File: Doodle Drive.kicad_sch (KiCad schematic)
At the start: 49 parts, among them J1 USB_B, J2 PINHD_1x4_Male, J6 PINHD_1x2_Male, SW1 Push_Button, SW2 Push_Button, SW3 Push_Button, U1 STM32F411RETx, U6 AP7343-30W5-7, U7 CP2102N-Axx-xQFN28, Y1 32.768KHz ±20ppm 12.5pF, Y2 25MHZ 9PF

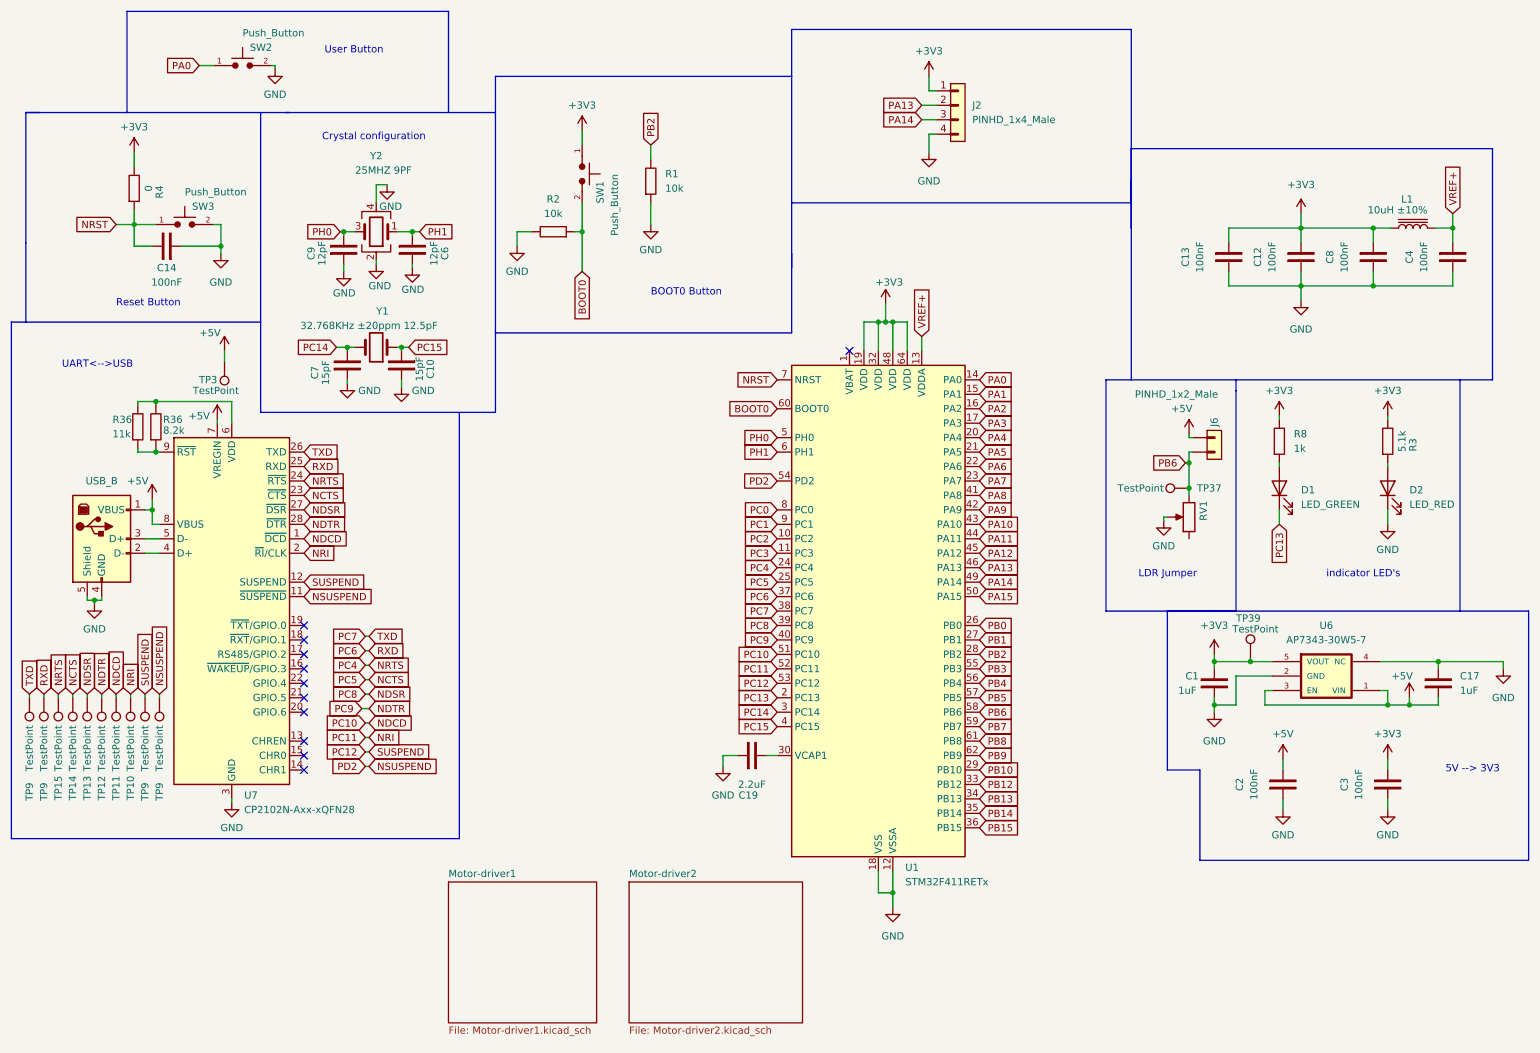
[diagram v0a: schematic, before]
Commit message: temporarly detached testpoints
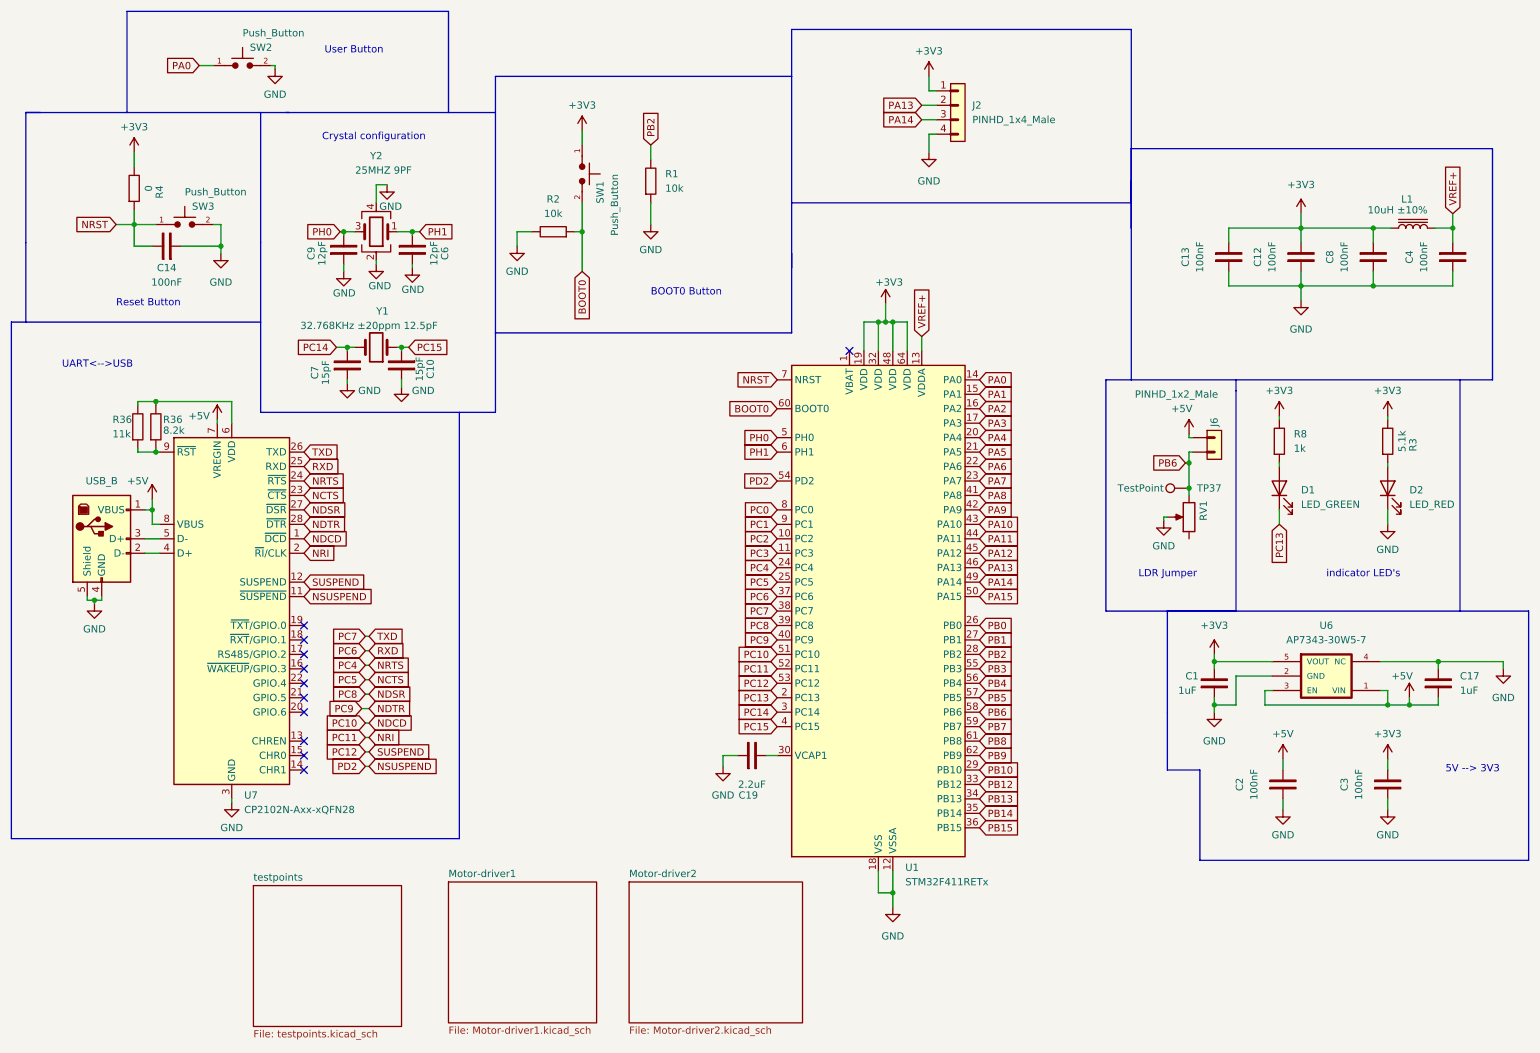
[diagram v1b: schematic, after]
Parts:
- removed TP10, TP11, TP12, TP13, TP14, TP15, TP3, TP39, TP9 (x4): TestPoint, TestPoint:TestPoint_Pad_D2.5mm, symbol Connector:TestPoint
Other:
- added sheet testpoints (testpoints.kicad_sch)

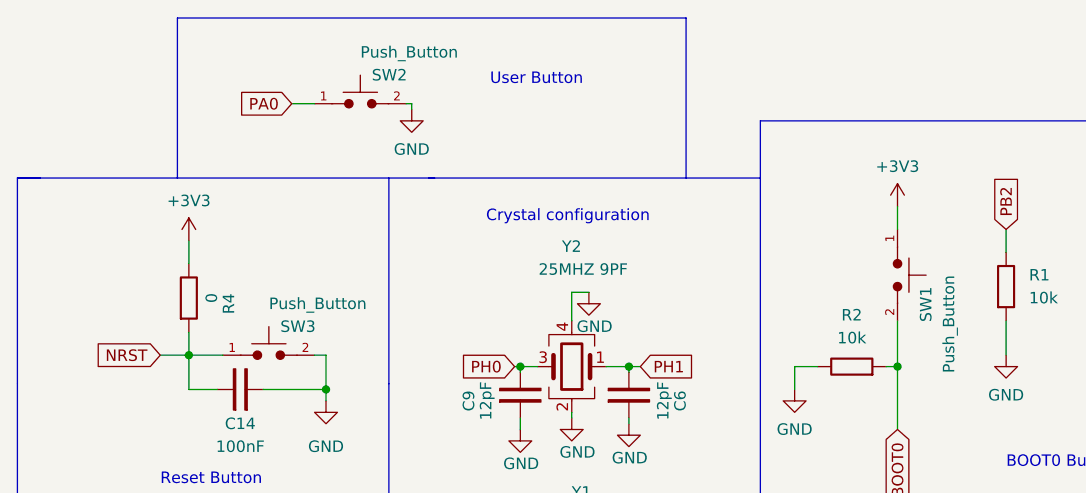
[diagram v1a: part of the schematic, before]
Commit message: routet Motor Driver modules, reattached and placed testpoints
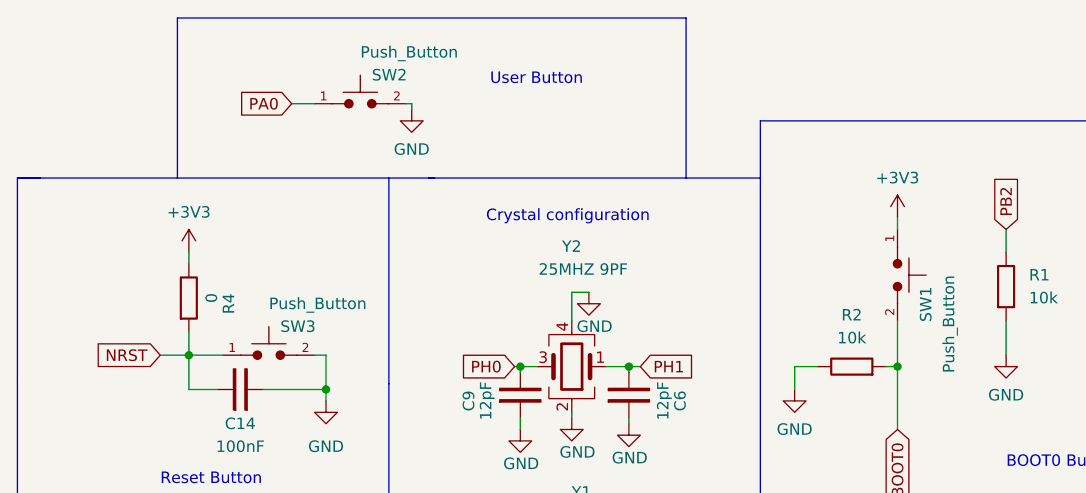
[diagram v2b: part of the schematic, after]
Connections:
- net +3.3V is gone; now on net +3V3: R4.2, SW1.1
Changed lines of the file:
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@@
-    (stroke (width 0) (type default))
-  )
-  (wire (pts (xy 37.465 40.005) (xy 37.465 37.465))
     (stroke (width 0) (type default))
   )
@@
     (stroke (width 0) (type default))
   )
+  (wire (pts (xy 116.205 34.925) (xy 116.205 36.195))
+    (stroke (width 0) (type default))
+  )
   (wire (pts (xy 266.7 127) (xy 266.7 128.27))
     (stroke (width 0) (type default))
@@
     (stroke (width 0) (type default))
   )
-  (wire (pts (xy 116.205 36.195) (xy 116.205 33.655))
-    (stroke (width 0) (type default))
-  )
   (wire (pts (xy 104.775 51.435) (xy 104.775 53.975))
     (stroke (width 0) (type default))
@@
   )
   (wire (pts (xy 86.36 51.435) (xy 83.82 51.435))
+    (stroke (width 0) (type default))
+  )
+  (wire (pts (xy 37.465 38.735) (xy 37.465 40.005))
     (stroke (width 0) (type default))
   )
@@
     )
   )
+  (symbol (lib_id "power:+3V3") (at 37.465 38.735 0) (unit 1)
+    (in_bom yes) (on_board yes) (dnp no) (fields_autoplaced)
+    (property "Reference" "#PWR024" (at 37.465 42.545 0)
+      (effects (font (size 1.27 1.27)) hide)
+    )
+    (property "Value" "+3V3" (at 37.465 34.29 0)
+      (effects (font (size 1.27 1.27)))
+    )
+    (property "Footprint" "" (at 37.465 38.735 0)
+      (effects (font (size 1.27 1.27)) hide)
+    )
+    (property "Datasheet" "" (at 37.465 38.735 0)
+      (effects (font (size 1.27 1.27)) hide)
+    )
+    (pin "1")
+    (instances
+      (project "Doodle Drive"
+        (path "/3ec634aa-8c09-482d-9325-2288a4dbd68b"
+          (reference "#PWR024") (unit 1)
+        )
+      )
+    )
+  )
   (symbol (lib_id "Device:Crystal") (at 80.01 71.755 180) (unit 1)
     (in_bom yes) (on_board yes) (dnp no)
@@
         (path "/3ec634aa-8c09-482d-9325-2288a4dbd68b"
           (reference "R2") (unit 1)
+        )
+      )
+    )
+  )
+  (symbol (lib_id "power:+3V3") (at 116.205 34.925 0) (unit 1)
+    (in_bom yes) (on_board yes) (dnp no) (fields_autoplaced)
+    (property "Reference" "#PWR020" (at 116.205 38.735 0)
+      (effects (font (size 1.27 1.27)) hide)
+    )
+    (property "Value" "+3V3" (at 116.205 30.48 0)
+      (effects (font (size 1.27 1.27)))
+    )
+    (property "Footprint" "" (at 116.205 34.925 0)
+      (effects (font (size 1.27 1.27)) hide)
+    )
+    (property "Datasheet" "" (at 116.205 34.925 0)
+      (effects (font (size 1.27 1.27)) hide)
+    )
+    (pin "1")
+    (instances
+      (project "Doodle Drive"
+        (path "/3ec634aa-8c09-482d-9325-2288a4dbd68b"
+          (reference "#PWR020") (unit 1)
         )
       )
@@
     )
   )
+  (symbol (lib_id "PCM_SL_Devices:Push_Button") (at 116.205 41.275 270) (unit 1)
+    (in_bom yes) (on_board yes) (dnp no)
+    (property "Reference" "SW1" (at 119.38 42.545 0)
+      (effects (font (size 1.27 1.27)) (justify left))
+    )
+    (property "Value" "Push_Button" (at 121.92 41.275 0)
+      (effects (font (size 1.27 1.27)) (justify left))
+    )
+    (property "Footprint" "Button_Switch_SMD:SW_SPST_B3U-1000P" (at 113.03 41.148 0)
+      (effects (font (size 1.27 1.27)) hide)
+    )
+    (property "Datasheet" "" (at 116.205 41.275 0)
+      (effects (font (size 1.27 1.27)) hide)
+    )
+    (pin "1")
+    (pin "2")
+    (instances
+      (project "Doodle Drive"
+        (path "/3ec634aa-8c09-482d-9325-2288a4dbd68b"
+          (reference "SW1") (unit 1)
+        )
+      )
+    )
+  )
   (symbol (lib_id "power:+5V") (at 40.64 98.425 0) (unit 1)
     (in_bom yes) (on_board yes) (dnp no)
@@
     )
   )
-  (symbol (lib_id "PCM_SL_Devices:Push_Button") (at 116.205 41.275 270) (unit 1)
-    (in_bom yes) (on_board yes) (dnp no)
-    (property "Reference" "SW1" (at 119.38 42.545 0)
-      (effects (font (size 1.27 1.27)) (justify left))
-    )
-    (property "Value" "Push_Button" (at 121.92 41.275 0)
-      (effects (font (size 1.27 1.27)) (justify left))
-    )
-    (property "Footprint" "Button_Switch_SMD:SW_SPST_B3U-1000P" (at 113.03 41.148 0)
-      (effects (font (size 1.27 1.27)) hide)
-    )
-    (property "Datasheet" "" (at 116.205 41.275 0)
-      (effects (font (size 1.27 1.27)) hide)
-    )
-    (pin "1")
-    (pin "2")
-    (instances
-      (project "Doodle Drive"
-        (path "/3ec634aa-8c09-482d-9325-2288a4dbd68b"
-          (reference "SW1") (unit 1)
-        )
-      )
-    )
-  )
   (symbol (lib_id "PCM_SL_Devices:Resistor") (at 38.1 85.725 90) (unit 1)
     (in_bom yes) (on_board yes) (dnp no)
@@
         (path "/3ec634aa-8c09-482d-9325-2288a4dbd68b"
           (reference "C9") (unit 1)
+        )
+      )
+    )
+  )
+  (symbol (lib_id "PCM_SL_Devices:Resistor") (at 37.465 43.815 90) (unit 1)
+    (in_bom yes) (on_board yes) (dnp no)
+    (property "Reference" "R4" (at 41.91 44.45 0)
+      (effects (font (size 1.27 1.27)))
+    )
+    (property "Value" "0" (at 40.005 43.815 0)
+      (effects (font (size 1.27 1.27)))
+    )
+    (property "Footprint" "Resistor_SMD:R_0805_2012Metric" (at 41.783 42.926 0)
+      (effects (font (size 1.27 1.27)) hide)
+    )
+    (property "Datasheet" "" (at 37.465 43.307 0)
+      (effects (font (size 1.27 1.27)) hide)
+    )
+    (pin "1")
+    (pin "2")
+    (instances
+      (project "Doodle Drive"
+        (path "/3ec634aa-8c09-482d-9325-2288a4dbd68b"
+          (reference "R4") (unit 1)
         )
       )
@@
     )
   )
-  (symbol (lib_id "power:+3.3V") (at 37.465 37.465 0) (unit 1)
-    (in_bom yes) (on_board yes) (dnp no) (fields_autoplaced)
-    (property "Reference" "#PWR024" (at 37.465 41.275 0)
-      (effects (font (size 1.27 1.27)) hide)
-    )
-    (property "Value" "+3V3" (at 37.465 33.02 0)
-      (effects (font (size 1.27 1.27)))
-    )
-    (property "Footprint" "" (at 37.465 37.465 0)
-      (effects (font (size 1.27 1.27)) hide)
-    )
-    (property "Datasheet" "" (at 37.465 37.465 0)
-      (effects (font (size 1.27 1.27)) hide)
-    )
-    (pin "1")
-    (instances
-      (project "Doodle Drive"
-        (path "/3ec634aa-8c09-482d-9325-2288a4dbd68b"
-          (reference "#PWR024") (unit 1)
-        )
-      )
-    )
-  )
   (symbol (lib_id "power:+3V3") (at 238.76 83.82 0) (unit 1)
     (in_bom yes) (on_board yes) (dnp no)
@@
         (path "/3ec634aa-8c09-482d-9325-2288a4dbd68b"
           (reference "#PWR011") (unit 1)
-        )
-      )
-    )
-  )
-  (symbol (lib_id "power:+3.3V") (at 116.205 33.655 0) (unit 1)
-    (in_bom yes) (on_board yes) (dnp no) (fields_autoplaced)
-    (property "Reference" "#PWR020" (at 116.205 37.465 0)
-      (effects (font (size 1.27 1.27)) hide)
-    )
-    (property "Value" "+3V3" (at 116.205 29.21 0)
-      (effects (font (size 1.27 1.27)))
-    )
-    (property "Footprint" "" (at 116.205 33.655 0)
-      (effects (font (size 1.27 1.27)) hide)
-    )
-    (property "Datasheet" "" (at 116.205 33.655 0)
-      (effects (font (size 1.27 1.27)) hide)
-    )
-    (pin "1")
-    (instances
-      (project "Doodle Drive"
-        (path "/3ec634aa-8c09-482d-9325-2288a4dbd68b"
-          (reference "#PWR020") (unit 1)
         )
       )
@@
         )
       )
-    )
-  )
-  (symbol (lib_id "PCM_SL_Devices:Resistor") (at 37.465 43.815 90) (unit 1)
-    (in_bom yes) (on_board yes) (dnp no)
-    (property "Reference" "R4" (at 41.91 44.45 0)
-      (effects (font (size 1.27 1.27)))
-    )
-    (property "Value" "0" (at 40.005 43.815 0)
-      (effects (font (size 1.27 1.27)))
-    )
-    (property "Footprint" "Resistor_SMD:R_0805_2012Metric" (at 41.783 42.926 0)
-      (effects (font (size 1.27 1.27)) hide)
-    )
-    (property "Datasheet" "" (at 37.465 43.307 0)
-      (effects (font (size 1.27 1.27)) hide)
-    )
-    (pin "1")
-    (pin "2")
-    (instances
-      (project "Doodle Drive"
-        (path "/3ec634aa-8c09-482d-9325-2288a4dbd68b"
-          (reference "R4") (unit 1)
-        )
-      )
